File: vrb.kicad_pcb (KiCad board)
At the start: 6 copper layers, 75 x 75 mm, 208 parts, among them J1 SM04B-GHS, J10 MiniFit, J11 XT30, J12 Mezzanine, J2 SM04B-GHS, J3 MiniFit, J4 MiniFit, J5 Pixhawk 1, J6 Pixhawk 2, J7 SM04B-GHS, J8 DEBUG, J9 SM04B-GHS, Q1 Q_NMOS_GSD, Q2 Q_NMOS_GSD, U1 STM32G0B1CBUx, U10 INA180A2, U11 TJA1051TK/3/1J, U12 I3A4W008A033V-001-R, U13 INA180A2, U14 TPS2121, U15 TPS2121, U16 TLV71333PDBVR, U17 TLA2528, U18 TPS2116DRL, U2 TJA1051TK/3/1J, U3 LMR51635, U4 INA180A2, U5 LMR51635, U6 INA180A2, U7 LMR51635, U8 INA180A2, U9 LMR51635, Y1 XRCGB16M000FXN20R0

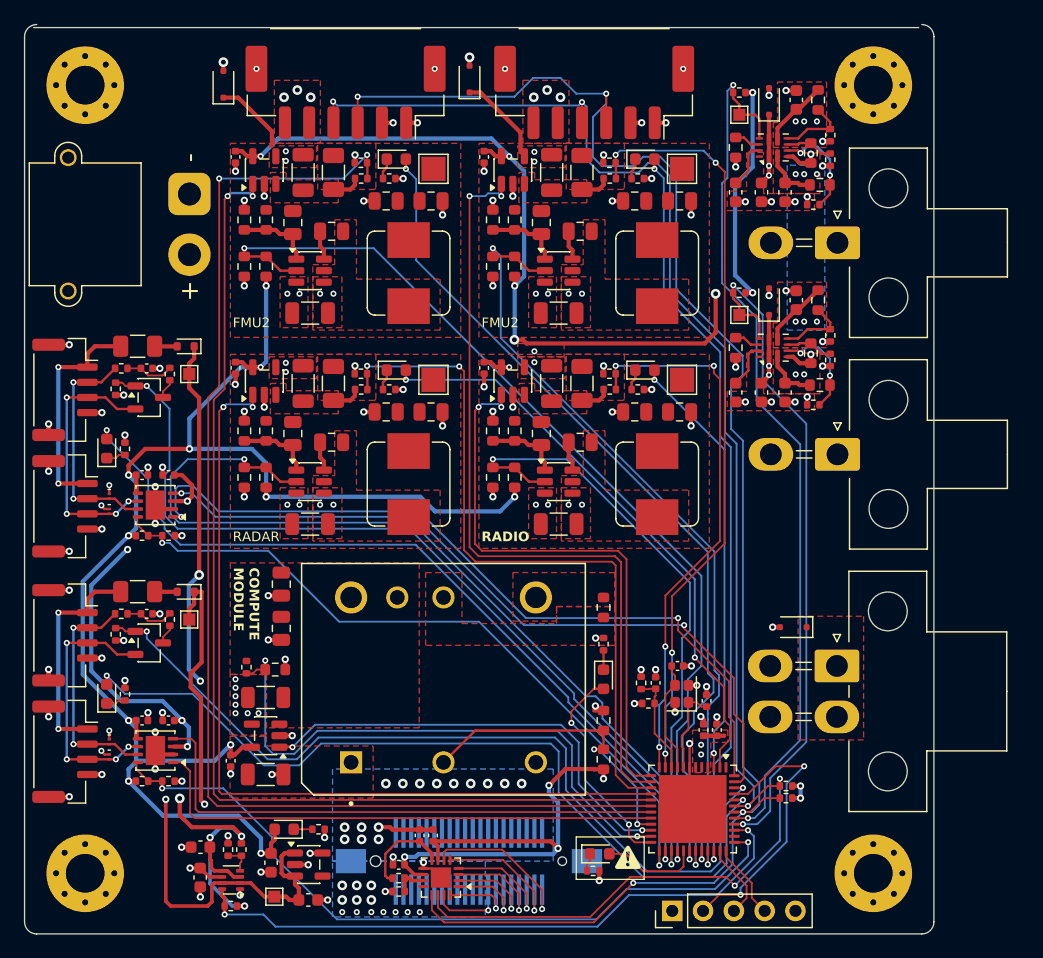
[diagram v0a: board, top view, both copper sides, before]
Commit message: fix capacitor sizes, clean up silkscreen, export
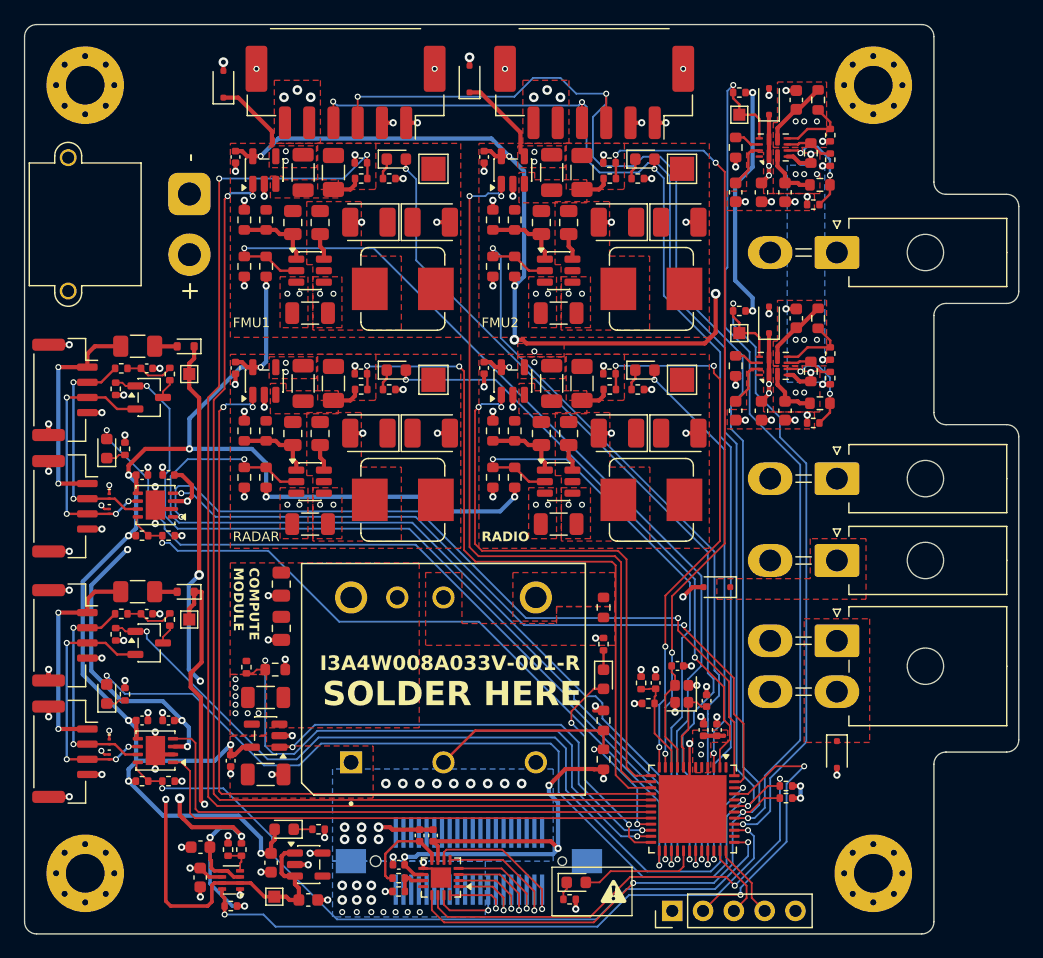
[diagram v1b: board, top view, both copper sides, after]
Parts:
- added D21: PZU24B2A, Diode_SMD:D_SOD-323F, F.Cu at (130.1, 106.4)
- added G***: LOGO, LOGO, B.Cu at (102.0, 77.4)
- added J13: MiniFit, Connector_Molex:Molex_Mini-Fit_Jr_5569-02A2_2x01_P4.20mm_Horizontal, F.Cu at (140.0, 104.2)
- C12, C13, C17, C18, C22, C23, C7, C8: value 22u -> 33u; footprint Capacitor_SMD:C_0805_2012Metric -> Capacitor_Tantalum_SMD:CP_EIA-3528-12_Kemet-T
- J10: footprint Connector_Molex:Molex_Mini-Fit_Jr_5569-04A1_2x02_P4.20mm_Horizontal -> Connector_Molex:Molex_Mini-Fit_Jr_5569-04A2_2x02_P4.20mm_Horizontal
- J3, J4: footprint Connector_Molex:Molex_Mini-Fit_Jr_5569-02A1_2x01_P4.20mm_Horizontal -> Connector_Molex:Molex_Mini-Fit_Jr_5569-02A2_2x01_P4.20mm_Horizontal
- L1, L2, L3, L4: value 15u -> 10u
- R17, R25, R33, R9: value 53K6 1% -> 56K1 1%
- moved D14 11.1 mm to (140.0, 120.2), turned to -90 degrees
- moved C17 5.42 mm to (121.9, 93.7), turned to 180 degrees
- moved C18 4.11 mm to (127.0, 93.7), turned to 0 degrees
- moved D20 3.05 mm to (118.5, 130.8)
- moved R78 3.05 mm to (118.0, 132.2)
- moved C13 2.26 mm to (121.9, 76.3)
- moved C22 2.26 mm to (101.4, 93.7)
- moved C8 2.26 mm to (101.4, 76.3)
- moved J10 2.08 mm to (140.0, 110.8)
- moved J3 2.00 mm to (140.0, 97.5)
- moved C12 1.75 mm to (127.0, 76.3)
- moved C23 1.75 mm to (106.5, 93.7)
- moved C7 1.75 mm to (106.5, 76.3)
- moved C30 1.50 mm to (136.7, 84.2)
- moved C31 1.50 mm to (135.7, 91.8)
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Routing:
- net GND: track 108.4 -> 110.5 mm, vias 147 -> 148
- net +3V3: track 329.4 -> 331.4 mm
- net /FAULT: track 8.18 -> 9.91 mm
- net /TELEM_STATUS: track 56.6 -> 55.1 mm
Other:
- board size 75 x 75 mm -> 82 x 75 mm
- board text added: "AUX"
- board text added: "CM"
- board text added: "Designed with in California"
- board text added: "FMU1"
- board text added: "I3A4W008A033V-001-R"
- board text added: "R1.0126"
- board text added: "SOLDER HERE"
- board text added: "TLM"
- board text removed: "COMPUTE"
- board text removed: "Designed with in California, USA"
- board text removed: "F*CKN'"
- board text removed: "READ THE DOCS"
- board text removed: "TELEM"

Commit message: minor revisions
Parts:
- added J14: Conn_01x02, Connector_PinHeader_2.54mm:PinHeader_1x02_P2.54mm_Vertical, F.Cu at (145.2, 84.5)
- added R79: 10K, Resistor_SMD:R_0402_1005Metric, F.Cu at (142.0, 83.2)
- added R81: 220K 1%, Resistor_SMD:R_0603_1608Metric, F.Cu at (142.8, 120.4)
- added R82: 1K, Resistor_SMD:R_0603_1608Metric, F.Cu at (142.8, 122.0)
- added R83: 10K 1%, Resistor_SMD:R_0603_1608Metric, F.Cu at (142.8, 123.6)
- added TP11: VBAT_SCALED, TestPoint:TestPoint_Pad_1.5x1.5mm, F.Cu at (145.8, 123.1)
- moved D14 1.52 mm to (138.7, 119.5), turned to 0 degrees
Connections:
- J10 pad 1: /CM_VOUT -> GND
- J10 pad 2: /CM_VOUT -> GND
- J10 pad 3: GND -> /CM_VOUT
- J10 pad 4: GND -> /CM_VOUT
- J13 pad 1: /RADAR_VOUT -> GND
- J13 pad 2: GND -> /RADAR_VOUT
- R43 pad 2: Net-(U12-VOUT-) -> GND
- U1 pad 38: unconnected-(U1-PD0-Pad38) -> /BUTTON
- U12 pad 4: Net-(U12-VOUT-) -> GND
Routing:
- net /BUTTON: track 0.00 -> 57.6 mm, vias 0 -> 1
- net /RESV2: track 13.4 -> 58.4 mm, vias 1 -> 4
- net +3V3: track 331.4 -> 340.4 mm, vias 29 -> 30
- net VBUS2: track 30.1 -> 26.9 mm
- net Net-(R81-Pad2): track 0.00 -> 3.20 mm
- net GND: track 110.5 -> 111.9 mm, vias 148 -> 149
- net +BATT: track 0.00 -> 0.78 mm, vias 21 -> 22
- removed copper zone on F.Cu, net Net-(U12-VOUT-)
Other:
- board text added: "+"
- board text added: "BTN"
- board text added: "C"
- board text added: "D"
- board text added: "Designed by Kalyan Sriram"
- board text added: "Docs"
- board text added: "G"
- board text added: "IN"
- board text added: "MCU PWR"
- board text added: "SWD Debug"
- board text added: "T"
- board text added: "TDK LAMBDA"
- board text added: "V"
